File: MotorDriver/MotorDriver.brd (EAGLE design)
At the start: 36.3 x 29.8 mm, 17 parts

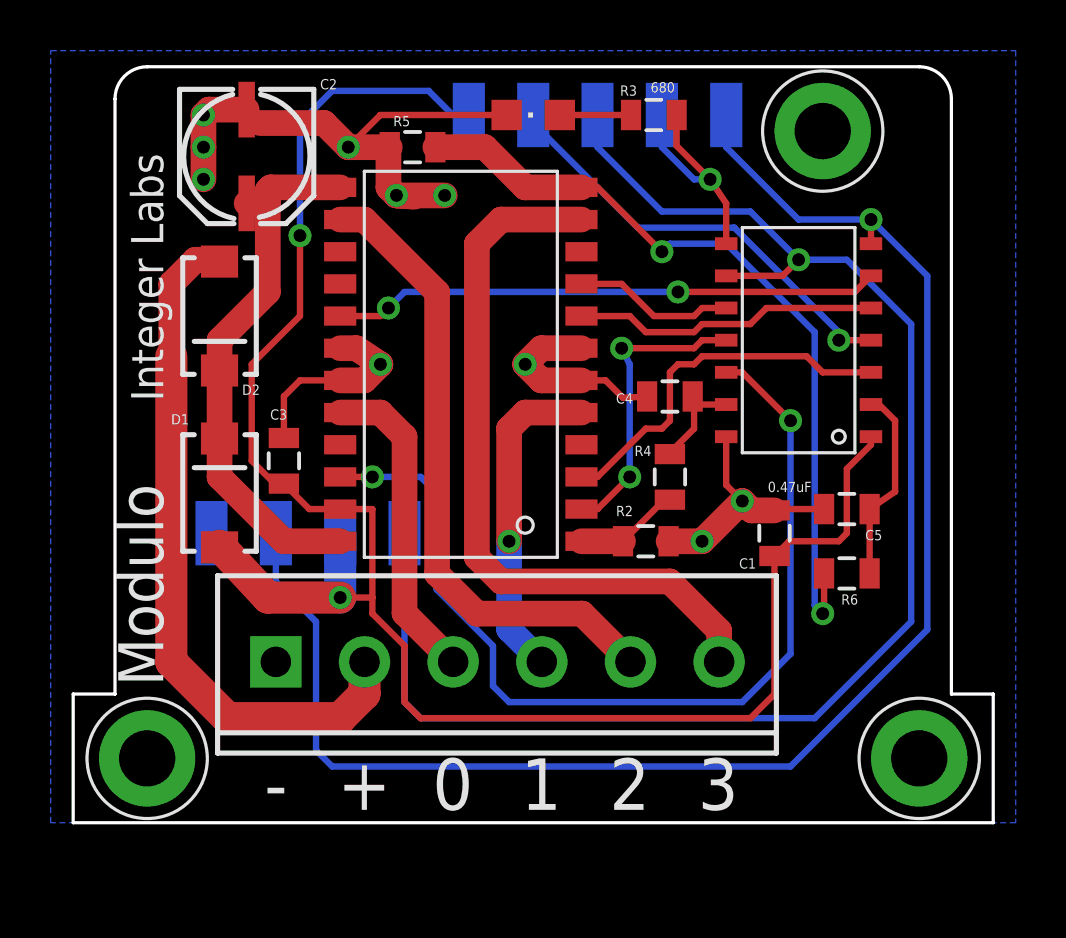
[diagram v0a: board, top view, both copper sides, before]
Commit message: Moved a bunch of files around
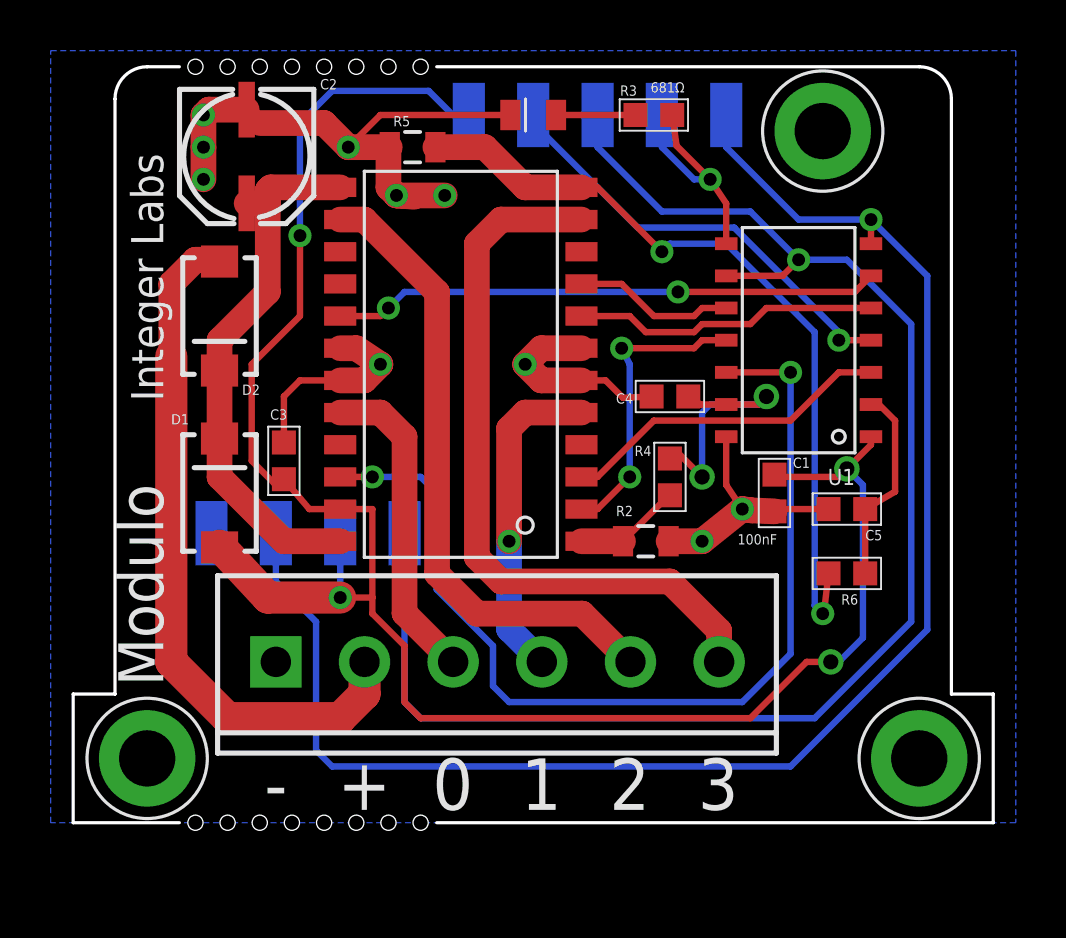
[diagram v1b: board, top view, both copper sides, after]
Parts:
- removed U$1: FOOTPRINTFOOTPRINT-2, IntegerLabs:FOOTPRINT2
- removed U$3: TINY841, IntegerLabs:SOIC14
- added PCB1: DEVICE-PCB-TABS, Modulo:DEVICE-PCB-TABS
- added U1: ATTINY841, Modulo:SOIC-14
- C1, C3, C4, C5: value 0.47uF -> 100nF; device SparkFun-Capacitors:0805 -> Modulo:0603
- LED: device adafruit:CHIPLED_0805 -> Modulo:0805-LED
- R2, R5: device SparkFun-Passives:0805 -> Modulo:0805
- R3: value 680 -> 681Ω; device SparkFun-Passives:0805 -> Modulo:0603
- R4, R6: value 2k -> 1.5KΩ; device SparkFun-Passives:0805 -> Modulo:0603
- moved C1 1.59 mm to (27.3, 13.0), turned to 90 degrees
- renumbered U$6 to U2
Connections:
- net ENABLEA: now also U1.3; no longer U$3.3
- net ENABLEB: now also U1.10; no longer U$3.10
- net GND: now also PCB1.BUS0, U1.14; no longer U$1.BUS0, U$3.14
- net IN0: now also U1.11; no longer U$3.11
- net IN1: now also U1.12; no longer U$3.12
- net IN2: now also U1.5; no longer U$3.5
- net IN3: now also U1.6; no longer U$3.6
- net MISO/LED: now also PCB1.PROG3, U1.8; no longer U$1.PROG3, U$3.8
- net RESET: now also PCB1.PROG1, U1.4; no longer U$1.PROG1, U$3.4
- net SCL/SCK: now also PCB1.BUS3, PCB1.PROG2, U1.9; no longer U$1.BUS3, U$1.PROG2, U$3.9
- net SDA/MOSI: now also PCB1.BUS1, PCB1.PROG4, U1.7; no longer U$1.BUS1, U$1.PROG4, U$3.7
- net SENSEA: now also U1.13; no longer U$3.13
- net SENSEB: now also U1.2; no longer U$3.2
- net VCC: now also PCB1.BUS2, PCB1.PROG0, U1.1; no longer U$1.BUS2, U$1.PROG0, U$3.1
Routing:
- net SENSEA: track 4.15 -> 10.8 mm, vias 0 -> 2
- net VCC: track 73.2 -> 77.4 mm, vias 2 -> 4
- net ENABLEA: track 14.8 -> 13.1 mm
- net IN1: track 37.9 -> 39.1 mm
- net GND: track 47.0 -> 47.5 mm
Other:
- outline, holes or cut-outs redrawn

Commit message: Major revision of all boards. Cleaned up old files. Exported BOM csv files for all boards
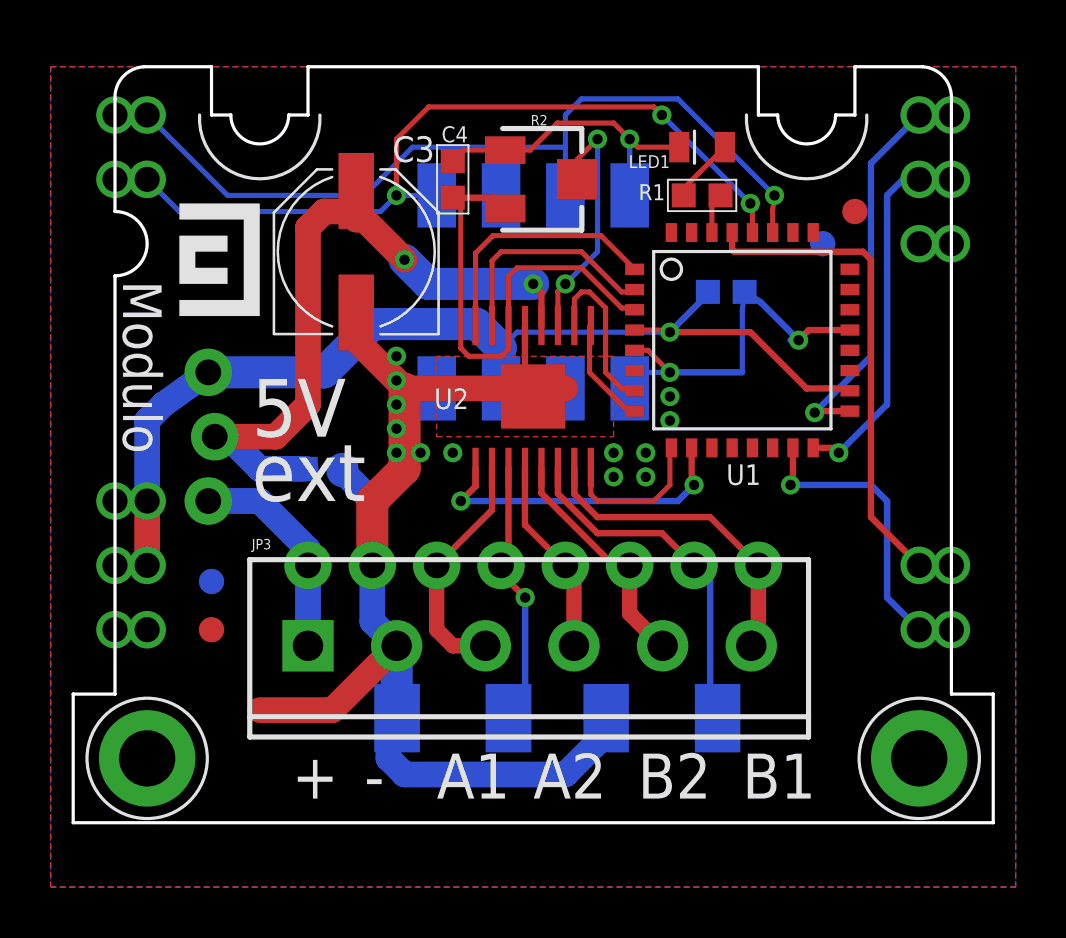
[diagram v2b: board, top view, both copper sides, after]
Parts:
- removed C5: 100nF, Modulo:0603
- removed D1, D2: (no value), SparkFun-DiscreteSemi:SMA-DIODE
- removed LED: blue, Modulo:0805-LED
- removed R5: .05, Modulo:0805
- removed R6: 1.5KΩ, Modulo:0603
- added F1, F2, F3, F4: FIDUCIAL, Modulo:FIDUCIAL_1MM
- added JP1: HEADER-1X4-AMPMODU, Modulo:AMPMODU-4P
- added JP2: (no value), SparkFun-Connectors:1X03_LOCK_NO_SILK
- added JP3: (no value), SparkFun-Connectors:SCREWTERMINAL-3.5MM-6
- added LED1: blue, Modulo:0805-LED
- added R1: 1KΩ, Modulo:0603
- added U$1, U$2: (no value), Modulo:LOGO-SMALL
- C1, C4: value 100nF -> .1uF
- C2: value (none) -> .1uF; device SparkFun-Capacitors:PANASONIC_C -> Modulo:0603
- C3: value 100nF -> 56uF; device Modulo:0603 -> Modulo:PANASONIC_D
- JP4: device SparkFun-Connectors:SCREWTERMINAL-3.5MM-6 -> SparkFun-Connectors:1X08_NO_SILK
- PCB1: value DEVICE-PCB-TABS -> DEVICE-PCB; device Modulo:DEVICE-PCB-TABS -> Modulo:DEVICE-PCB
- R2: value .05 -> TRIMPOT; device Modulo:0805 -> Modulo:TRIMPOT-3MM
- R3: value 681Ω -> .25Ω; device Modulo:0603 -> SparkFun-Resistors:R2010
- R4: value 1.5KΩ -> .25Ω; device Modulo:0603 -> SparkFun-Resistors:R2010
- U1: value ATTINY841 -> ATTINY48/88-TQFP; device Modulo:SOIC-14 -> Modulo:TQFP-32
- U2: value NJM2670 -> DRV8848; device IntegerLabs:SOP-24-E3 -> Modulo:HTSSOP-16
- moved R3 23.8 mm to (22.9, 4.13), flipped to the bottom
- moved JP4 19.4 mm to (26.7, 10.2), flipped to the bottom
- moved R2 14.9 mm to (18.1, 25.4), turned to 270 degrees
- moved R4 12.8 mm to (14.6, 4.13), flipped to the bottom, turned to 0 degrees
- moved C2 12.7 mm to (9.53, 14.0), flipped to the bottom, turned to 180 degrees
- moved C4 12.1 mm to (14.6, 25.4), turned to 90 degrees
- moved C3 8.74 mm to (10.8, 22.5)
- moved C1 8.16 mm to (25.4, 21.0), flipped to the bottom, turned to 180 degrees
- moved U1 4.26 mm to (26.0, 19.1), turned to 0 degrees
- moved U2 2.62 mm to (17.8, 16.8), turned to 0 degrees
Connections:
- removed net ENABLEA: U1.3, U2.3
- removed net ENABLEB: U1.10, U2.9
- removed net IN0: U1.11, U2.2
- removed net IN1: U1.12, U2.22
- removed net IN2: U1.5, U2.8
- removed net IN3: U1.6, U2.17
- removed net MISO/LED: PCB1.PROG3, R3.2, U1.8
- removed net N$2: R2.2, R4.2, U2.1
- removed net N$3: R5.2, R6.2, U2.12
- removed net N$5: LED.A, R3.1
- removed net OUT0: JP4.4, U2.5
- removed net OUT1: JP4.3, U2.20
- removed net OUT2: JP4.5, U2.14
- removed net OUT3: JP4.6, U2.11
- removed net SCL/SCK: PCB1.BUS3, PCB1.PROG2, U1.9
- removed net SDA/MOSI: PCB1.BUS1, PCB1.PROG4, U1.7
- removed net SENSEA: C4.1, R4.1, U1.13
- removed net SENSEB: C5.1, R6.1, U1.2
- removed net TSD: U2.16
- removed net VS: C2.+, D1.C, D2.C, U2.13, U2.24
- new net AIN1: U1.1, U2.16
- new net AIN2: U1.2, U2.15
- new net AOUT1: JP3.3, JP4.6, U2.2
- new net AOUT2: JP3.4, JP4.4, U2.4
- new net ASENSE: JP4.5, R4.1, U2.3
- new net BIN1: U1.8, U2.9
- new net BIN2: U1.7, U2.10
- new net BOUT1: JP3.6, JP4.1, U2.7
- new net BOUT2: JP3.5, JP4.3, U2.5
- new net BSENSE: JP4.2, R3.1, U2.6
- new net LED: R1.2, U1.30
- new net MISO: PCB1.MISO, U1.16
- new net MOSI: PCB1.MOSI, U1.15
- new net N$10: C2.1, C3.+, JP2.2, U2.12
- new net N$7: LED1.A, R1.1
- new net NFAULT: U1.9, U2.8
- new net NSLEEP: U1.10, U2.1
- new net SCK: PCB1.CLK, U1.17
- new net SCL: JP1.P$7, JP1.P$8, PCB1.SCL, U1.28
- new net SDA: JP1.P$3, JP1.P$4, PCB1.SDA, U1.27
- new net VINT: C4.1, R2.3, U1.3, U2.14
- new net VREF: R2.2, U2.11
- net GND: now also C1.2, C2.2, C3.-, JP1.P$1, JP1.P$2, JP3.2, JP4.7, LED1.C, PCB1.GND, R3.2, R4.2, U1.21, U1.5, U2.13, U2.PAD; no longer C1.1, C2.-, C3.2, C5.2, JP4.1, LED.C, PCB1.BUS0, R5.1, U1.14, U2.18, U2.19, U2.6, U2.7
- net RESET: now also PCB1.RESET, U1.29; no longer PCB1.PROG1, U1.4
- net VCC: now also C1.1, JP1.P$5, JP1.P$6, JP2.1, PCB1.VCC, PCB1.VPROG, U1.18, U1.4; no longer C1.2, C3.1, D1.A, PCB1.BUS2, PCB1.PROG0, U1.1, U2.23
- net VIN: now also JP2.3, JP3.1, JP4.8; no longer D2.A, JP4.2
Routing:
- net SDA/MOSI: track 62.1 -> 0.00 mm, vias 1 -> 0
- net SCL/SCK: track 60.6 -> 0.00 mm, vias 1 -> 0
- net IN1: track 39.1 -> 0.00 mm, vias 2 -> 0
- net VCC: track 77.4 -> 41.9 mm, vias 4 -> 1
- net SDA: track 0.00 -> 33.4 mm, vias 0 -> 1
- net SCL: track 0.00 -> 31.7 mm, vias 0 -> 3
- net N$3: track 31.1 -> 0.00 mm, vias 2 -> 0
- net GND: track 47.5 -> 77.1 mm, vias 10 -> 16
- net OUT3: track 28.9 -> 0.00 mm
- net N$10: track 0.00 -> 28.4 mm, vias 0 -> 2
- net OUT2: track 25.2 -> 0.00 mm
- net VS: track 21.7 -> 0.00 mm
- net IN3: track 21.6 -> 0.00 mm, vias 2 -> 0
- net VINT: track 0.00 -> 19.1 mm
- net VIN: track 27.5 -> 8.54 mm
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- added copper zone on layer 1, net GND
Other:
- outline, holes or cut-outs redrawn
- board text added: "5V"
- board text added: "A1"
- board text added: "A2"
- board text added: "B1"
- board text added: "B2"
- board text added: "ext"
- board text removed: "0"
- board text removed: "1"
- board text removed: "2"
- board text removed: "3"

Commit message: New diode selections
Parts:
- added D1: DIODE-SCHOTTKY, Modulo:SMP
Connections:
- new net N$1: D1.C, JP2.1
- net VCC: now also D1.A; no longer JP2.1
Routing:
- net N$1: track 0.00 -> 4.91 mm
- net VCC: track 41.9 -> 43.7 mm

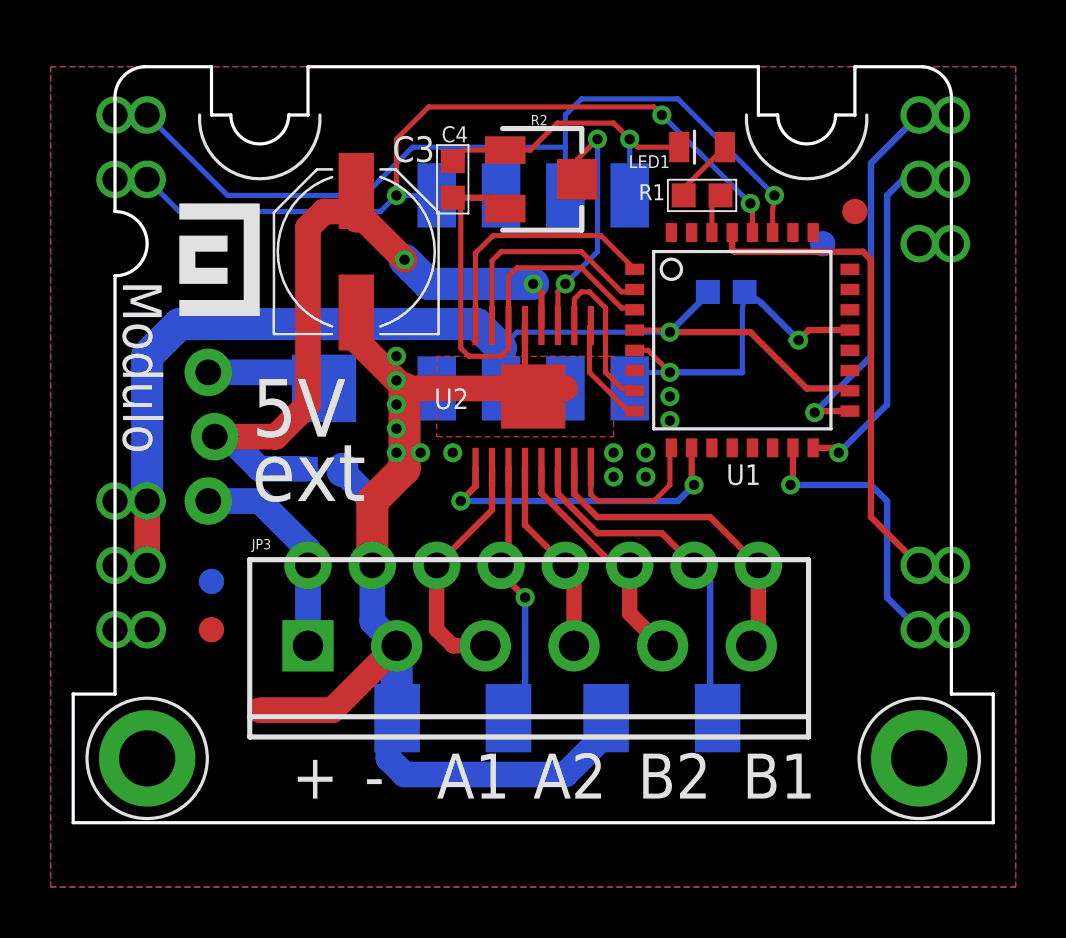
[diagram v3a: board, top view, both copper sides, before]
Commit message: Check point of current PCB designs. Among other things I think this change includes rewiring of programming lines on many of the boards,.
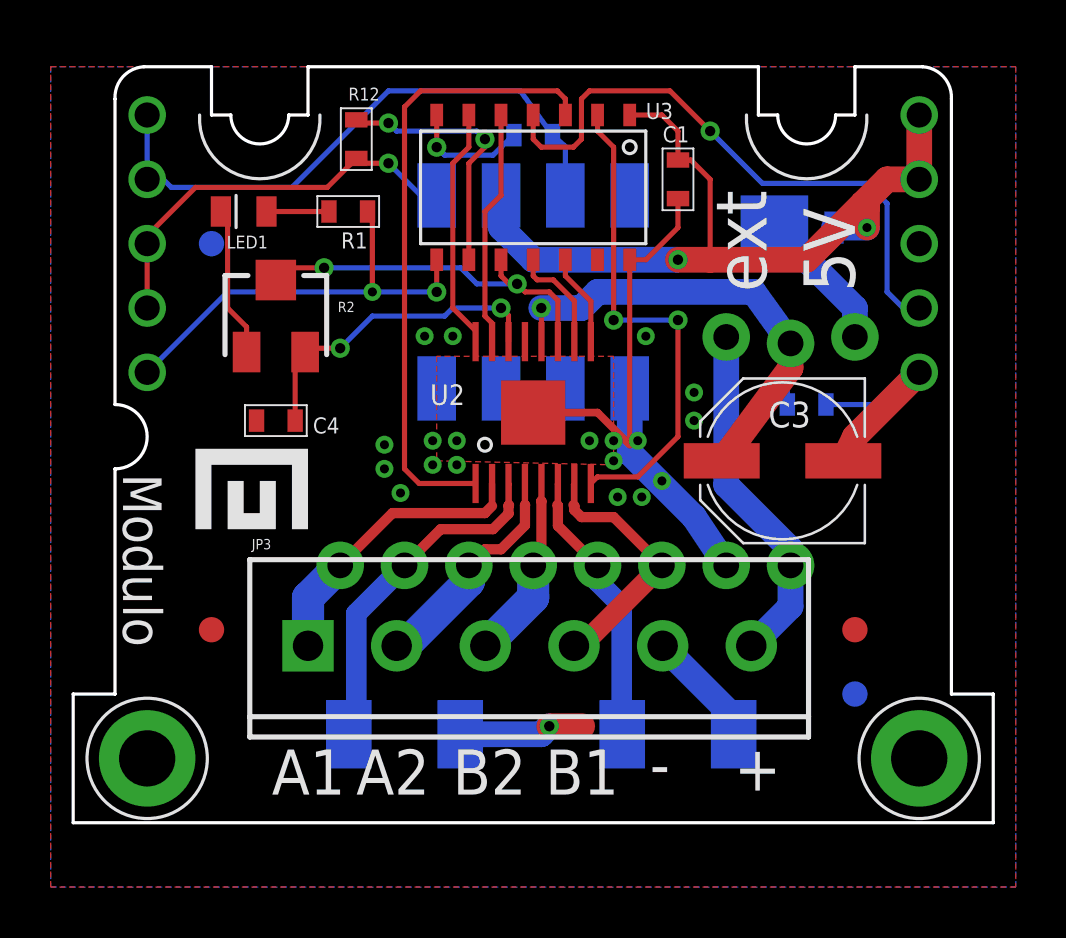
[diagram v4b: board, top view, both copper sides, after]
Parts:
- removed U1: ATTINY48/88-TQFP, Modulo:TQFP-32
- added R12, R13: 150Ω, Modulo:0603
- added U3: ATTINY841, Modulo:SOIC-14
- moved F3 30.3 mm to (5.08, 7.62)
- moved JP2 25.4 mm to (30.5, 19.1), turned to 0 degrees
- moved F4 25.4 mm to (30.5, 7.62)
- moved C2 19.2 mm to (28.6, 16.5)
- moved D1 18.9 mm to (27.3, 23.5), turned to 180 degrees
- moved C3 18.7 mm to (27.6, 14.3), turned to 180 degrees
- moved LED1 18.3 mm to (6.35, 24.1)
- moved F1 17.8 mm to (30.5, 5.08)
- moved R1 14.0 mm to (10.5, 24.1)
- moved F2 13.3 mm to (5.08, 22.9)
- moved C4 11.8 mm to (7.62, 15.9), turned to 180 degrees
- moved R2 11.8 mm to (7.62, 20.0), turned to 0 degrees
- moved U$1 10.5 mm to (6.35, 12.2), turned to 0 degrees
- moved U$2 8.67 mm to (7.94, 14.0), turned to 0 degrees
- moved C1 4.84 mm to (23.5, 25.4), flipped to the top, turned to 270 degrees
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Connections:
- removed net LED: R1.2, U1.30
- removed net MISO: PCB1.MISO, U1.16
- removed net MOSI: PCB1.MOSI, U1.15
- removed net SCK: PCB1.CLK, U1.17
- new net MISO/LED: PCB1.MISO, R1.2, U3.8
- new net SCL/SCK: R12.2, U3.9
- new net SDA/MOSI: R13.2, U3.7
- net AIN1: now also U3.6; no longer U1.1
- net AIN2: now also U3.5; no longer U1.2
- net AOUT1: now also JP3.1, JP4.8; no longer JP3.3, JP4.6
- net AOUT2: now also JP3.2, JP4.6; no longer JP3.4, JP4.4
- net ASENSE: now also JP4.7; no longer JP4.5
- net BIN1: now also U3.12; no longer U1.8
- net BIN2: now also U3.11; no longer U1.7
- net BOUT1: now also JP3.4, JP4.3; no longer JP3.6, JP4.1
- net BOUT2: now also JP3.3, JP4.5; no longer JP3.5, JP4.3
- net BSENSE: now also JP4.4; no longer JP4.2
- net GND: now also JP3.5, JP4.2, U3.14; no longer JP3.2, JP4.7, U1.21, U1.5
- net NFAULT: now also U3.2; no longer U1.9
- net NSLEEP: now also U3.3; no longer U1.10
- net RESET: now also U3.4; no longer U1.29
- net SCL: now also PCB1.CLK, R12.1; no longer U1.28
- net SDA: now also PCB1.MOSI, R13.1; no longer U1.27
- net VCC: now also U3.1; no longer U1.18, U1.4
- net VIN: now also JP3.6, JP4.1; no longer JP3.1, JP4.8
- net VINT: no longer U1.3
- net VREF: now also U3.10
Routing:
- net GND: track 77.1 -> 49.1 mm, vias 16 -> 20
- net MISO/LED: track 0.00 -> 17.3 mm, vias 0 -> 2
- net SCL: track 31.7 -> 16.2 mm, vias 3 -> 1
- net SCK: track 14.9 -> 0.00 mm, vias 1 -> 0
- net NFAULT: track 6.05 -> 19.7 mm, vias 0 -> 2
- net MISO: track 13.6 -> 0.00 mm, vias 1 -> 0
- net NSLEEP: track 12.5 -> 24.7 mm, vias 2 -> 0
- net MOSI: track 11.2 -> 0.00 mm, vias 1 -> 0
- net VCC: track 43.7 -> 32.6 mm, vias 1 -> 2
- net SCL/SCK: track 0.00 -> 10.4 mm, vias 0 -> 2
- net SDA: track 33.4 -> 23.8 mm, vias 1 -> 0
- net N$10: track 28.4 -> 20.5 mm, vias 2 -> 1
- net VINT: track 19.1 -> 12.8 mm, vias 0 -> 2
- net VIN: track 8.54 -> 13.9 mm
- net SDA/MOSI: track 0.00 -> 4.77 mm, vias 0 -> 1
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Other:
- outline, holes or cut-outs redrawn

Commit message: Various changes
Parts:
- removed JP4: (no value), SparkFun-Connectors:1X08_NO_SILK
- removed R2: TRIMPOT, Modulo:TRIMPOT-3MM
- added SJ1, SJ2, SJ3: SOLDERJUMPERNO, SparkFun-Passives:SJ_2S-NO
- added U1: MCP4013, Modulo:SOT-23-6
- C4: value .1uF -> 10uF
- moved F1 23.7 mm to (24.1, 27.9)
- moved U$2 21.6 mm to (29.1, 9.53)
- moved R13 18.7 mm to (4.45, 14.0), turned to 90 degrees
- moved U$1 15.8 mm to (17.1, 23.8)
- moved F2 15.4 mm to (5.08, 7.46)
- moved F4 14.8 mm to (21.4, 19.4)
- moved U3 13.4 mm to (8.26, 24.1), turned to 270 degrees
- moved LED1 11.6 mm to (17.5, 27.3), turned to 270 degrees
- moved C1 6.28 mm to (17.5, 27.1), flipped to the bottom, turned to 180 degrees
- moved JP2 5.09 mm to (25.4, 19.4), flipped to the top
- moved C4 4.96 mm to (11.4, 12.7), turned to 270 degrees
- moved R1 4.49 mm to (13.7, 27.3), turned to 180 degrees
- moved D1 2.54 mm to (24.8, 23.5)
- moved R12 2.09 mm to (12.9, 27.3), flipped to the bottom, turned to 0 degrees
- moved U2 1.59 mm to (17.8, 14.6)
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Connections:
- new net CS: U1.4, U3.10
- new net UD: U1.3, U3.13
- net AOUT1: no longer JP4.8
- net AOUT2: no longer JP4.6
- net ASENSE: now also SJ3.2; no longer JP4.7
- net BOUT1: no longer JP4.3
- net BOUT2: no longer JP4.5
- net BSENSE: now also SJ2.2; no longer JP4.4
- net GND: now also SJ2.1, SJ3.1, U1.2; no longer JP4.2, R2.1
- net VCC: now also U1.1
- net VIN: no longer JP4.1
- net VINT: now also SJ1.1, U1.6; no longer R2.3
- net VREF: now also SJ1.2, U1.5; no longer R2.2, U3.10
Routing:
- net VCC: track 32.6 -> 52.3 mm, vias 2 -> 4
- net SDA: track 23.8 -> 42.0 mm, vias 0 -> 2
- net RESET: track 23.8 -> 41.7 mm, vias 1 -> 2
- net CS: track 0.00 -> 13.9 mm, vias 0 -> 2
- net VREF: track 14.9 -> 27.5 mm, vias 2 -> 4
- net UD: track 0.00 -> 12.5 mm, vias 0 -> 2
- net NFAULT: track 19.7 -> 30.9 mm, vias 2 -> 4
- net VINT: track 12.8 -> 22.2 mm
- net BIN1: track 3.65 -> 12.9 mm
- net SCL: track 16.2 -> 24.5 mm
- net N$10: track 20.5 -> 28.0 mm, vias 1 -> 2
- net BIN2: track 4.28 -> 11.3 mm
- net ASENSE: track 13.7 -> 19.7 mm, vias 0 -> 1
- net BOUT1: track 10.2 -> 5.49 mm
- net GND: track 49.1 -> 53.0 mm, vias 20 -> 24
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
